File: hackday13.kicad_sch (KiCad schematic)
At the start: 3 parts

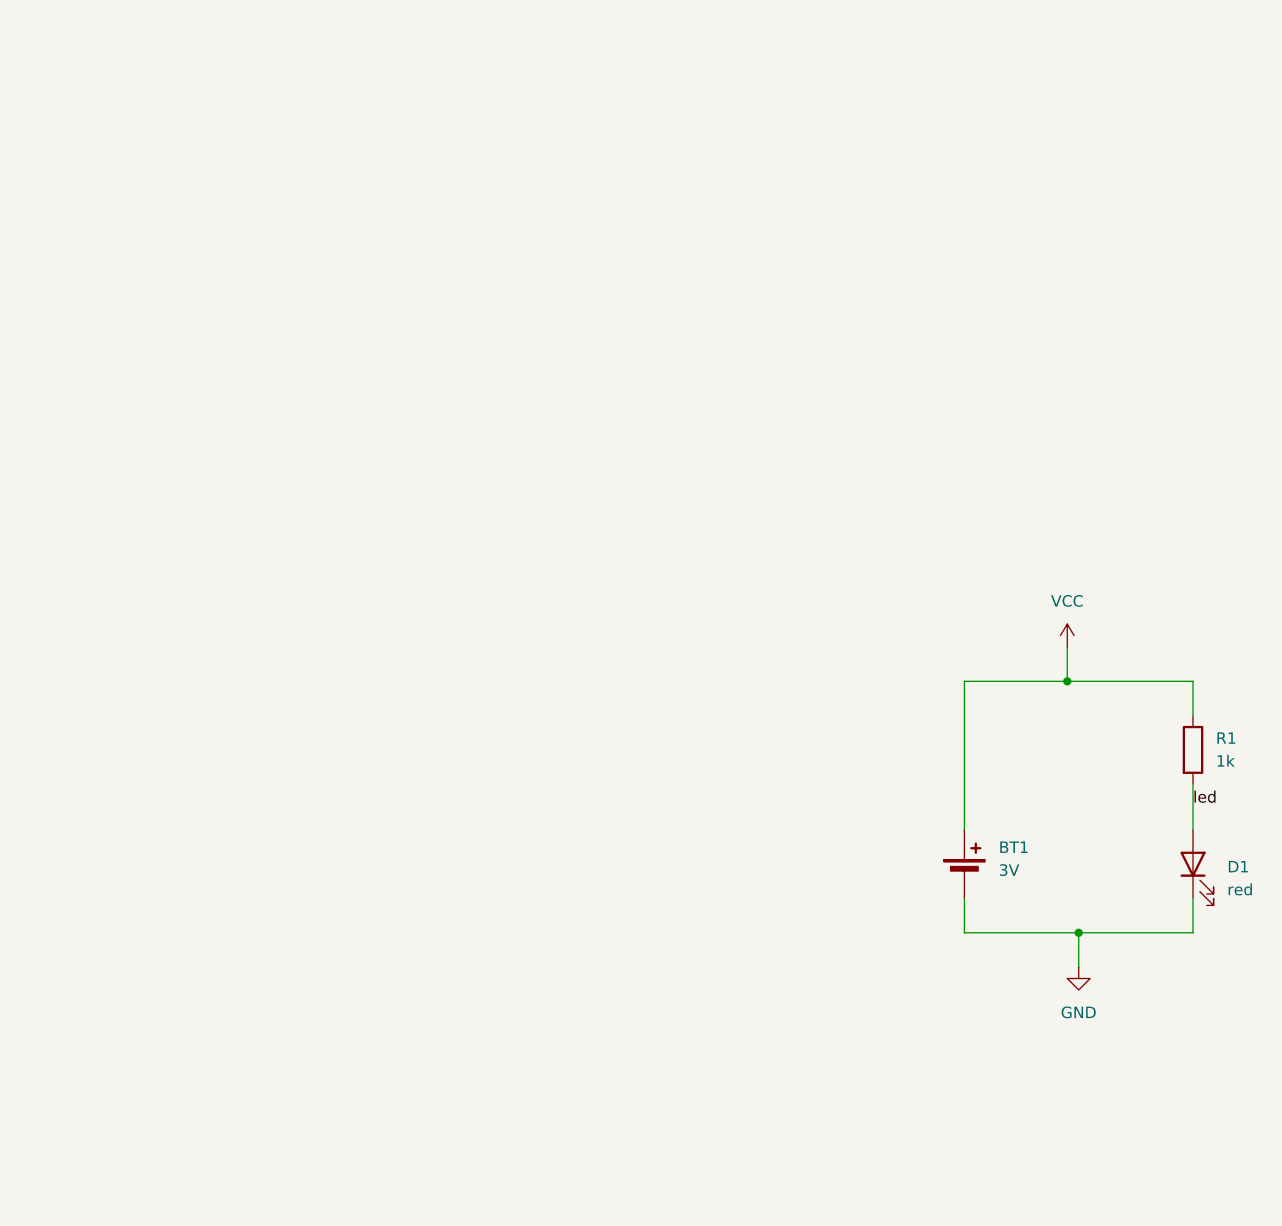
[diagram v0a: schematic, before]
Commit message: First pass at adding PICO and connecting to Pmod
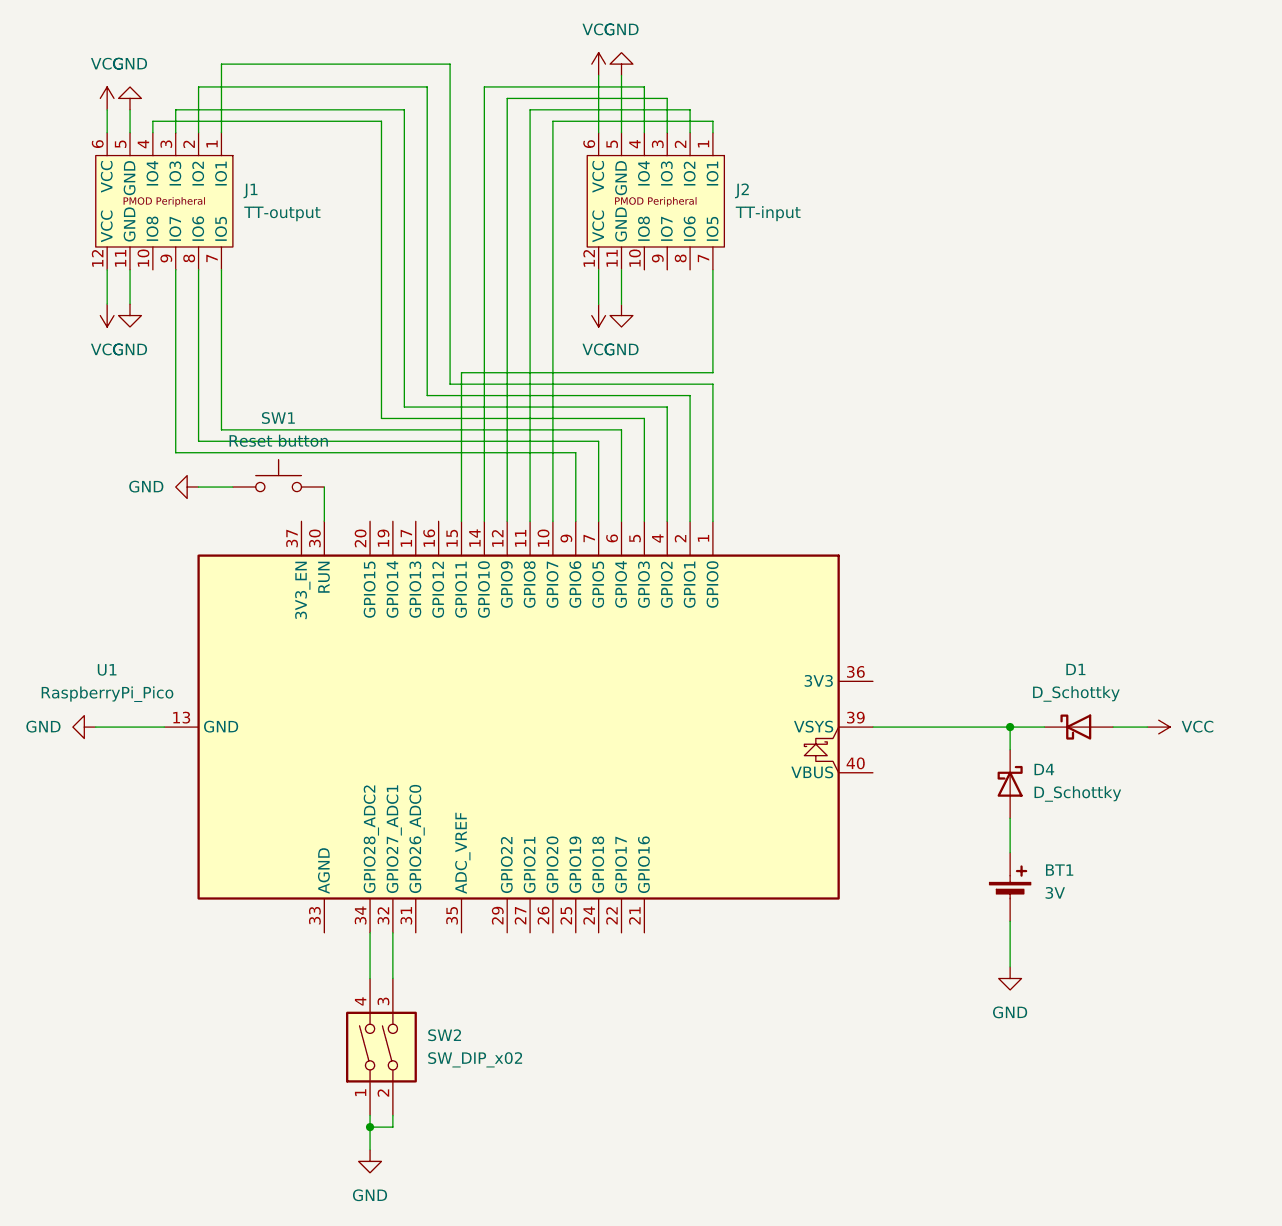
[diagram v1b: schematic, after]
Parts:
- removed D1: red, LED_THT:LED_D5.0mm, symbol Device:LED
- removed R1: 1k, Resistor_THT:R_Axial_DIN0309_L9.0mm_D3.2mm_P12.70mm_Horizontal, symbol Device:R
- added D1, D4: D_Schottky, Diode_THT:D_DO-35_SOD27_P7.62mm_Horizontal, symbol Device:D_Schottky
- added J1: TT-output, TinyTapeout:PinHeader_2x06_P2.54mm_PMODPeriph2B, symbol TinyTapeout:PMOD_PERIPH_2x6
- added J2: TT-input, TinyTapeout:PinHeader_2x06_P2.54mm_PMODPeriph2B, symbol TinyTapeout:PMOD_PERIPH_2x6
- added SW1: Reset button, Button_Switch_THT:SW_PUSH_6mm, symbol Switch:SW_Push
- added SW2: SW_DIP_x02, symbol Switch:SW_DIP_x02
- added U1: RaspberryPi_Pico, Module_RaspberryPi_Pico:RaspberryPi_Pico_Common, symbol MCU_Module_RaspberryPi_Pico:RaspberryPi_Pico
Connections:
- net GND: now also J1.11 (GND), J1.5 (GND), J2.11 (GND), J2.5 (GND), SW1.1, SW2.1, SW2.2, U1.13 (GND), U1.18 (GND), U1.23 (GND), U1.28 (GND), U1.3 (GND), U1.38 (GND), U1.8 (GND)
- net VCC: now also D1.2 (A), J1.12 (VCC), J1.6 (VCC), J2.12 (VCC), J2.6 (VCC); no longer BT1.1 (+)
- new net: SW1.2, U1.30 (RUN)
- new net: D1.1 (K), D4.1 (K), U1.39 (VSYS)
- new net: BT1.1 (+), D4.2 (A)
- new net: SW2.3, U1.32 (GPIO27_ADC1)
- new net: SW2.4, U1.34 (GPIO28_ADC2)
- new net: J1.1 (IO1), U1.1 (GPIO0)
- new net: J1.2 (IO2), U1.2 (GPIO1)
- new net: J1.3 (IO3), U1.4 (GPIO2)
- new net: J1.4 (IO4), U1.5 (GPIO3)
- new net: J1.7 (IO5), U1.6 (GPIO4)
- new net: J1.8 (IO6), U1.7 (GPIO5)
- new net: J1.9 (IO7), U1.9 (GPIO6)
- new net: J2.1 (IO1), U1.10 (GPIO7)
- new net: J2.2 (IO2), U1.11 (GPIO8)
- new net: J2.3 (IO3), U1.12 (GPIO9)
- new net: J2.4 (IO4), U1.14 (GPIO10)
- new net: J2.7 (IO5), U1.15 (GPIO11)
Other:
- moved on the sheet: BT1

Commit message: Add LED dot matrix schematic
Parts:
- added LEDs1: LED dot matrix 12 pin, symbol custom_components_led_pcb:TA07-11SEKWA
- added R1, R2, R3, R4, R5: R, symbol Device:R
- BT1: footprint Battery:BatteryHolder_Keystone_105_1x2430 -> Battery:BatteryHolder_Keystone_3002_1x2032
- SW2: footprint (none) -> Button_Switch_THT:SW_DIP_SPSTx02_Slide_9.78x7.26mm_W7.62mm_P2.54mm
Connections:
- net at U1.16 (GPIO12): now also R1.2
- net at U1.17 (GPIO13): now also R2.2
- net at U1.19 (GPIO14): now also R3.2
- net at U1.20 (GPIO15): now also R4.2
- net at U1.21 (GPIO16): now also R5.2
- net at U1.22 (GPIO17): now also LEDs1.12 (R1)
- net at U1.24 (GPIO18): now also LEDs1.11 (R2)
- net at U1.25 (GPIO19): now also LEDs1.2 (R3)
- net at U1.26 (GPIO20): now also LEDs1.9 (R4)
- net at U1.27 (GPIO21): now also LEDs1.4 (R5)
- net at U1.29 (GPIO22): now also LEDs1.5 (R6)
- net at U1.31 (GPIO26_ADC0): now also LEDs1.6 (R7)
- new net: LEDs1.3 (C2), R2.1
- new net: LEDs1.10 (C3), R3.1
- new net: LEDs1.1 (C1), R1.1
- new net: LEDs1.7 (C4), R4.1
- new net: LEDs1.8 (C5), R5.1
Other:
- moved on the sheet: BT1, D1, D4, SW1, SW2

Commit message: Add footprint for LED dot matrix
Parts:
- LEDs1: footprint (none) -> custom_components_led_pcb:LED_dot_matrix_TA07-11SEKWA
- R1, R2, R3, R4, R5: value R -> 200 Ohm; footprint (none) -> Resistor_THT:R_Axial_DIN0207_L6.3mm_D2.5mm_P10.16mm_Horizontal
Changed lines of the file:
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@@
 			)
 		)
-		(property "Value" "R"
+		(property "Value" "200 Ohm"
 			(at 252.73 107.95 90)
 			(effects
@@
 			)
 		)
-		(property "Footprint" ""
+		(property "Footprint" "Resistor_THT:R_Axial_DIN0207_L6.3mm_D2.5mm_P10.16mm_Horizontal"
 			(at 252.73 113.538 90)
 			(effects
@@
 			)
 		)
-		(property "Value" "R"
+		(property "Value" "200 Ohm"
 			(at 252.73 110.49 90)
 			(effects
@@
 			)
 		)
-		(property "Footprint" ""
+		(property "Footprint" "Resistor_THT:R_Axial_DIN0207_L6.3mm_D2.5mm_P10.16mm_Horizontal"
 			(at 252.73 116.078 90)
 			(effects
@@
 			)
 		)
-		(property "Value" "R"
+		(property "Value" "200 Ohm"
 			(at 252.73 105.41 90)
 			(effects
@@
 			)
 		)
-		(property "Footprint" ""
+		(property "Footprint" "Resistor_THT:R_Axial_DIN0207_L6.3mm_D2.5mm_P10.16mm_Horizontal"
 			(at 252.73 110.998 90)
 			(effects
@@
 			)
 		)
-		(property "Value" "R"
+		(property "Value" "200 Ohm"
 			(at 252.73 113.03 90)
 			(effects
@@
 			)
 		)
-		(property "Footprint" ""
+		(property "Footprint" "Resistor_THT:R_Axial_DIN0207_L6.3mm_D2.5mm_P10.16mm_Horizontal"
 			(at 252.73 118.618 90)
 			(effects
@@
 			)
 		)
-		(property "Value" "R"
+		(property "Value" "200 Ohm"
 			(at 252.73 115.57 90)
 			(effects
@@
 			)
 		)
-		(property "Footprint" ""
+		(property "Footprint" "Resistor_THT:R_Axial_DIN0207_L6.3mm_D2.5mm_P10.16mm_Horizontal"
 			(at 252.73 121.158 90)
 			(effects
@@
 			)
 		)
-		(property "Footprint" ""
+		(property "Footprint" "custom_components_led_pcb:LED_dot_matrix_TA07-11SEKWA"
 			(at 237.49 109.22 0)
 			(effects

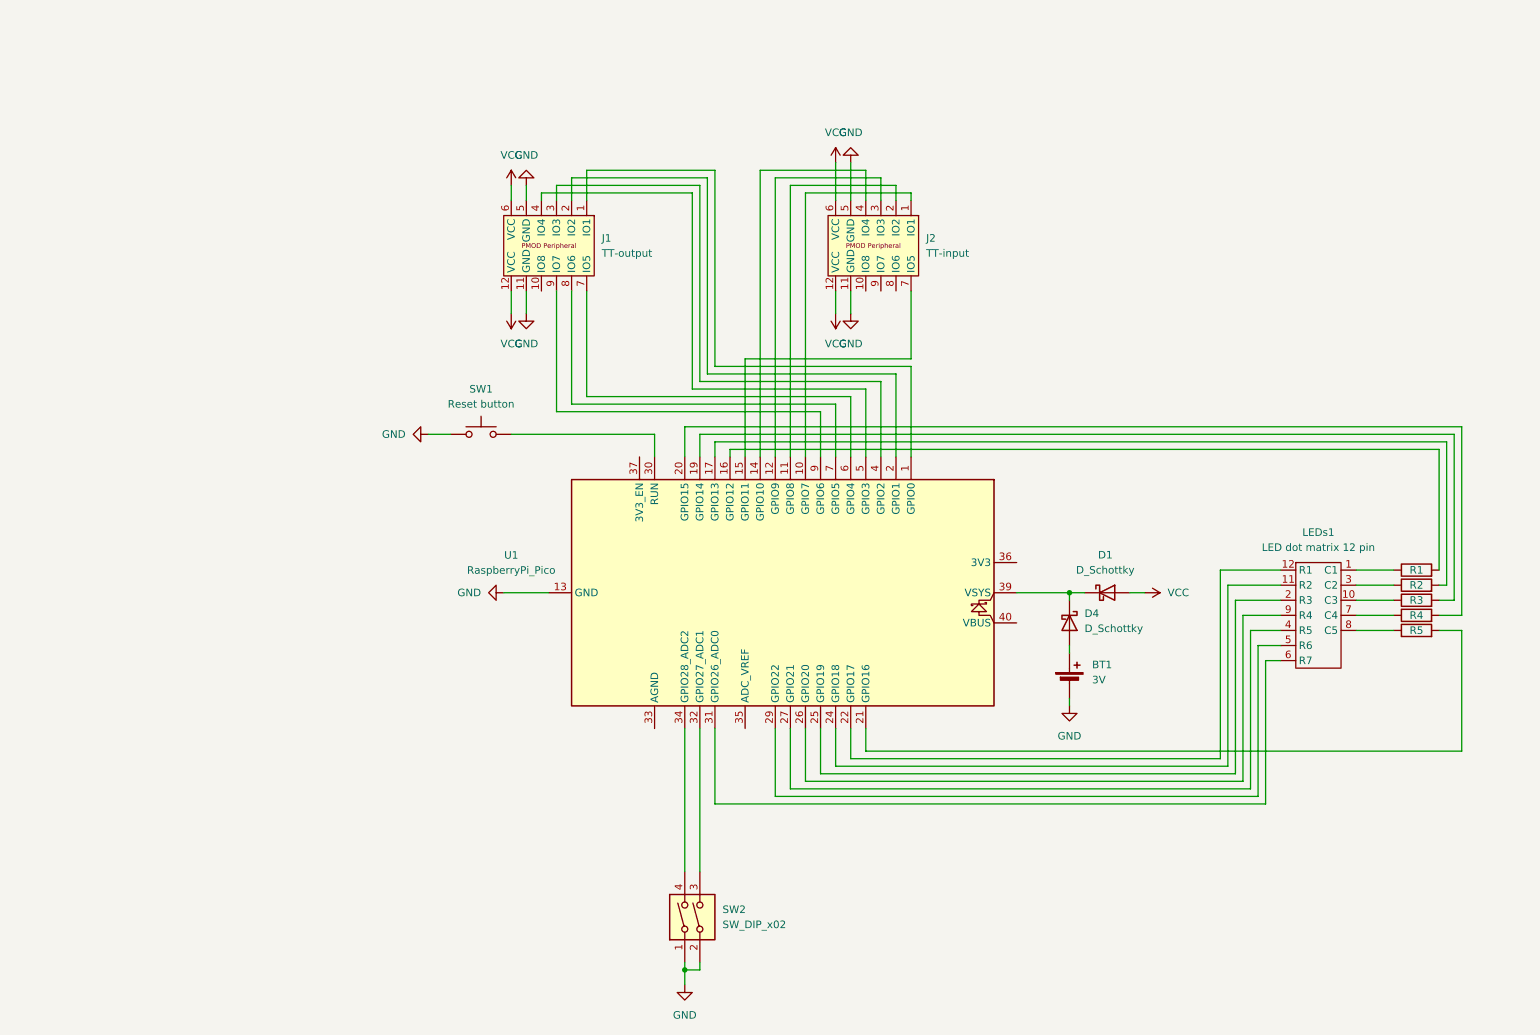
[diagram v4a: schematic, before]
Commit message: Connect up shift registers in schematic
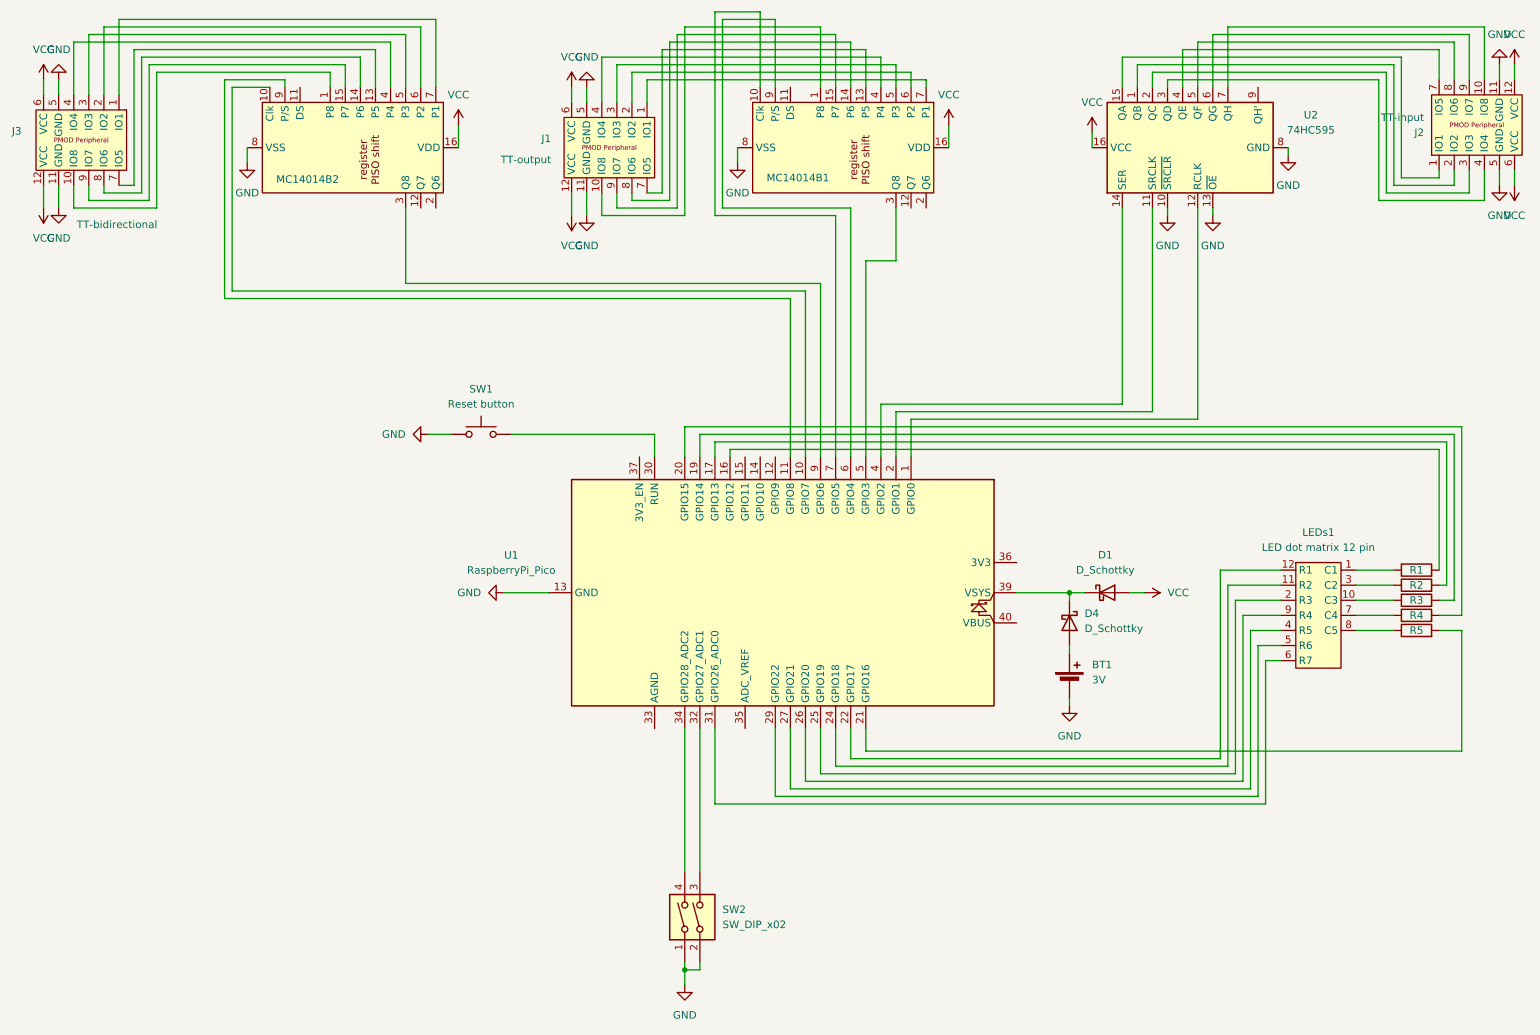
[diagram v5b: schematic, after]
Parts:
- added J3: TT-bidirectional, TinyTapeout:PinHeader_2x06_P2.54mm_PMODPeriph2B, symbol TinyTapeout:PMOD_PERIPH_2x6
- added MC14014B1, MC14014B2: ~, symbol custom_components_led_pcb:MC14014B
- added U2: 74HC595, symbol 74xx:74HC595
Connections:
- net GND: now also J3.11 (GND), J3.5 (GND), MC14014B1.8 (VSS), MC14014B2.8 (VSS), U2.10 (~{SRCLR}), U2.13 (~{OE}), U2.8 (GND)
- net VCC: now also J3.12 (VCC), J3.6 (VCC), MC14014B1.16 (VDD), MC14014B2.16 (VDD), U2.16 (VCC)
- net at U1.1 (GPIO0): now also U2.12 (RCLK); no longer J1.1 (IO1)
- net at J1.10 (IO8): now also MC14014B1.1 (P8)
- net at U1.2 (GPIO1): now also U2.11 (SRCLK); no longer J1.2 (IO2)
- net at U1.4 (GPIO2): now also U2.14 (SER); no longer J1.3 (IO3)
- net at J1.4 (IO4): now also MC14014B1.4 (P4); no longer U1.5 (GPIO3)
- net at J1.7 (IO5): now also MC14014B1.13 (P5); no longer U1.6 (GPIO4)
- net at J1.8 (IO6): now also MC14014B1.14 (P6); no longer U1.7 (GPIO5)
- net at U1.9 (GPIO6): now also MC14014B2.3 (Q8); no longer J1.9 (IO7)
- net at U1.10 (GPIO7): now also MC14014B2.10 (Clk); no longer J2.1 (IO1)
- net at J2.10 (IO8): now also U2.7 (QH)
- net at U1.11 (GPIO8): now also MC14014B2.9 (P/S); no longer J2.2 (IO2)
- net at J2.3 (IO3): now also U2.2 (QC); no longer U1.12 (GPIO9)
- net at J2.4 (IO4): now also U2.3 (QD); no longer U1.14 (GPIO10)
- net at J2.7 (IO5): now also U2.4 (QE); no longer U1.15 (GPIO11)
- net at J2.8 (IO6): now also U2.5 (QF)
- net at J2.9 (IO7): now also U2.6 (QG)
- new net: J3.10 (IO8), MC14014B2.1 (P8)
- new net: J3.7 (IO5), MC14014B2.13 (P5)
- new net: J3.8 (IO6), MC14014B2.14 (P6)
- new net: J3.9 (IO7), MC14014B2.15 (P7)
- new net: J3.4 (IO4), MC14014B2.4 (P4)
- new net: J3.3 (IO3), MC14014B2.5 (P3)
- new net: J3.2 (IO2), MC14014B2.6 (P2)
- new net: J3.1 (IO1), MC14014B2.7 (P1)
- new net: J2.2 (IO2), U2.1 (QB)
- new net: J2.1 (IO1), U2.15 (QA)
- new net: J1.1 (IO1), MC14014B1.7 (P1)
- new net: J1.2 (IO2), MC14014B1.6 (P2)
- new net: J1.3 (IO3), MC14014B1.5 (P3)
- new net: J1.9 (IO7), MC14014B1.15 (P7)
- new net: MC14014B1.10 (Clk), U1.7 (GPIO5)
- new net: MC14014B1.3 (Q8), U1.5 (GPIO3)
- new net: MC14014B1.9 (P/S), U1.6 (GPIO4)
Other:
- title: Hackday 13 -> Hackday 13 & 14
- moved on the sheet: J1, J2

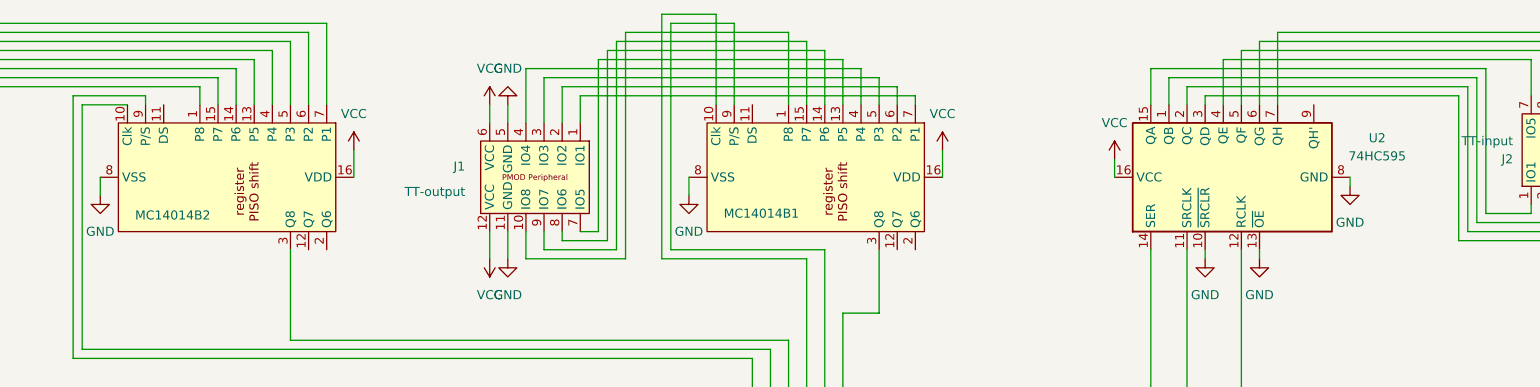
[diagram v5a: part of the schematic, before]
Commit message: Add schematics for shift regs
Some other cleanup like wires and component names.
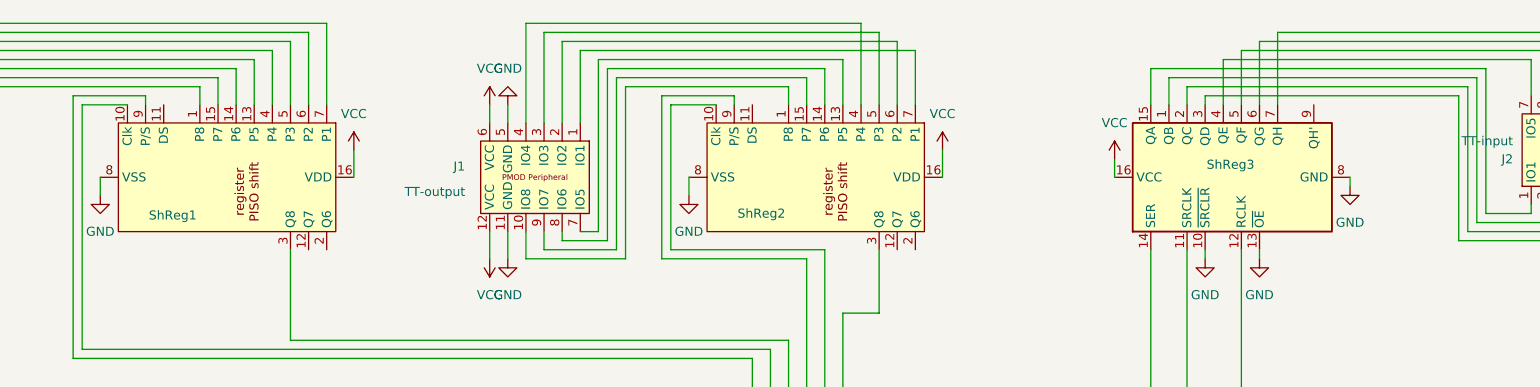
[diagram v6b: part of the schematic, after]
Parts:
- ShReg1: renamed from MC14014B2; value ~ -> MC14014B; footprint (none) -> Package_SO:SOIC-16_3.9x9.9mm_P1.27mm
- ShReg2: renamed from MC14014B1; value ~ -> MC14014B; footprint (none) -> Package_SO:SOIC-16_3.9x9.9mm_P1.27mm
- ShReg3: renamed from U2; footprint (none) -> Package_SO:SOIC-16_3.9x9.9mm_P1.27mm
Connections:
- net at ShReg2.10 (Clk): now also U1.6 (GPIO4); no longer U1.7 (GPIO5)
- net at ShReg2.9 (P/S): now also U1.7 (GPIO5); no longer U1.6 (GPIO4)
